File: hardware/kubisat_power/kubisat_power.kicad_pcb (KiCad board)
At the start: 2 copper layers, 80 x 80 mm, 83 parts, among them J1 USB_C_Receptacle_PowerOnly_6P, J2 B2B-PH-SM4-TB_LF__SN_, J3 B2B-PH-SM4-TB_LF__SN_, J4 B2B-PH-SM4-TB_LF__SN_, J5 B2B-PH-SM4-TB_LF__SN_, J6 Conn_01x04_Pin, J7 Conn_01x04_Pin, J8 Conn_01x04_Pin, Q1 Si2305, SW1 SW_Wuerth_450301014042, U2 INA3221, U3 LN2220, U4 CN3791, U5 TP4056, U6 DW01A, U7 FS8205

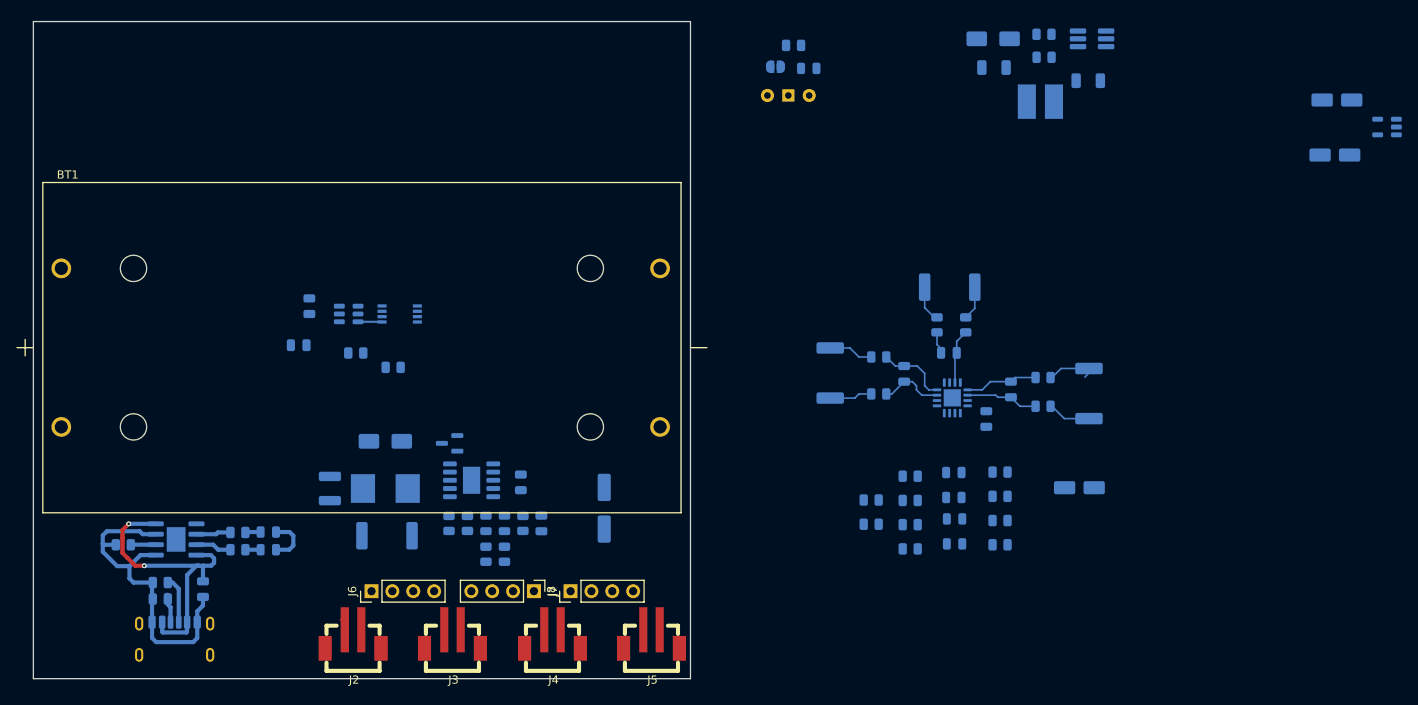
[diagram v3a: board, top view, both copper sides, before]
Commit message: arranged elements on board, made some traces
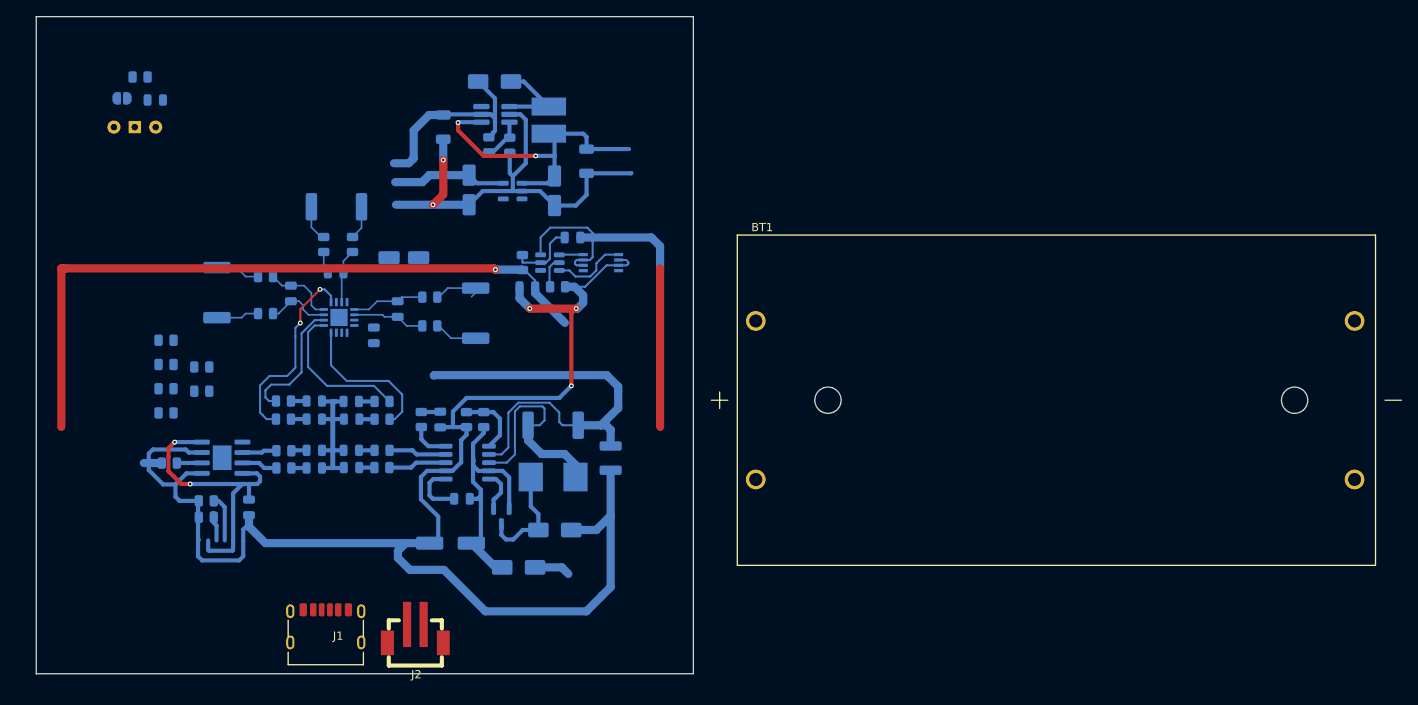
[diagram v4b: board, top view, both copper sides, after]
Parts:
- removed J3, J4, J5: B2B-PH-SM4-TB_LF__SN_, kubisat:B2B-PH-SM4-TB_LF__SN_
- removed J6, J7, J8: Conn_01x04_Pin, Connector_PinHeader_2.54mm:PinHeader_1x04_P2.54mm_Vertical
- added D12: SS14, Diode_SMD:D_SMA, B.Cu at (77.1, 84.2)
- J1: moved to F.Cu
- moved U1 106.7 mm to (76.4, 38.3)
- moved C8 105.5 mm to (71.1, 38.2), turned to -90 degrees
- moved C2 95.9 mm to (81.5, 38.3), turned to -90 degrees
- moved R27 92.1 mm to (34.2, 56.5)
- moved R28 92.1 mm to (34.2, 59.5)
- moved R29 92.1 mm to (34.2, 62.4)
- moved R30 92.1 mm to (34.2, 65.3)
- moved R36 89.0 mm to (48.5, 63.9)
- moved R33 87.5 mm to (48.5, 66.1)
- moved C7 86.9 mm to (63.1, 46.5)
- moved BT1 84.8 mm to (142.6, 63.8)
- moved R31 83.1 mm to (38.5, 59.8)
- moved R32 83.1 mm to (38.5, 62.7)
- moved D11 79.7 mm to (32.9, 27.2)
- moved JP1 79.7 mm to (28.8, 27.1)
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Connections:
- C2 pad 1: 5V_SENSE_OUT -> SOLAR_SENSE_OUT
- D10 pad 2: Net-(D10-A) -> INFO_LED_ENABLE
- D4 pad 2: Net-(D4-A) -> INFO_LED_ENABLE
- D5 pad 2: Net-(D5-A) -> INFO_LED_ENABLE
- D7 pad 2: Net-(D7-A) -> INFO_LED_ENABLE
- D8 pad 2: Net-(D8-A) -> INFO_LED_ENABLE
- D9 pad 2: Net-(D9-A) -> INFO_LED_ENABLE
- J2 pad 1: Net-(J6-Pin_3) -> GND
- J2 pad 2: VS -> Net-(D12-A)
- R23 pad 1: INFO_LED_ENABLE -> Net-(D4-K)
- R23 pad 2: Net-(D4-A) -> Net-(U4-~{DONE})
- R24 pad 1: INFO_LED_ENABLE -> Net-(D5-K)
- R24 pad 2: Net-(D5-A) -> Net-(U4-~{CHRG})
- R27 pad 1: Net-(D10-K) -> Net-(U2-PV)
- R28 pad 1: Net-(D9-K) -> Net-(U2-CRITICAL)
- R29 pad 1: Net-(D8-K) -> Net-(U2-WARNING)
- R30 pad 1: Net-(D7-K) -> Net-(U2-TC)
- R33 pad 1: INFO_LED_ENABLE -> Net-(D7-K)
- R33 pad 2: Net-(D7-A) -> Net-(U2-TC)
- R34 pad 1: INFO_LED_ENABLE -> Net-(D8-K)
- R34 pad 2: Net-(D8-A) -> Net-(U2-WARNING)
- R35 pad 1: INFO_LED_ENABLE -> Net-(D9-K)
- R35 pad 2: Net-(D9-A) -> Net-(U2-CRITICAL)
- R36 pad 1: INFO_LED_ENABLE -> Net-(D10-K)
- R36 pad 2: Net-(D10-A) -> Net-(U2-PV)
- U1 pad 1: 5V_SENSE_OUT -> SOLAR_SENSE_OUT
- U2 pad 10: Net-(D10-K) -> Net-(U2-PV)
- U2 pad 13: Net-(D7-K) -> Net-(U2-TC)
- U2 pad 8: Net-(D8-K) -> Net-(U2-WARNING)
- U2 pad 9: Net-(D9-K) -> Net-(U2-CRITICAL)
- U4 pad 3: Net-(D5-K) -> Net-(U4-~{CHRG})
- U4 pad 4: Net-(D4-K) -> Net-(U4-~{DONE})
- U7 pad 1: Net-(U6-GND) -> unconnected-(U7-D1-Pad1)
- U7 pad 2: unconnected-(U7-D12-Pad2) -> Net-(U6-GND)
- U7 pad 3: GND -> Net-(U6-GND)
- U7 pad 4: Net-(U6-OC) -> Net-(U6-OD)
- U7 pad 5: unconnected-(U7-D12-Pad5) -> Net-(U6-OC)
- U7 pad 6: Net-(U6-OD) -> GND
- U7 pad 7: (no net) -> GND
- U7 pad 8: (no net) -> unconnected-(U7-D2-Pad8)
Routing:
- net GND: track 40.9 -> 254.6 mm, vias 0 -> 5
- net SOLAR_SENSE_OUT: track 9.69 -> 132.4 mm, vias 0 -> 3
- net SOLAR_SENSE_IN: track 5.46 -> 58.0 mm
- net Net-(U6-GND): track 2.94 -> 49.9 mm
- net VS: track 1.47 -> 33.0 mm
- net Net-(U4-CSP): track 0.00 -> 26.8 mm
- net 5V_SENSE_IN: track 5.30 -> 30.8 mm
- net Net-(U2-TC): track 0.00 -> 24.0 mm, vias 0 -> 2
- net INFO_LED_ENABLE: track 5.82 -> 27.0 mm
- net Net-(U2-CRITICAL): track 0.00 -> 18.1 mm
- net Net-(U2-WARNING): track 0.00 -> 18.1 mm
- net Net-(U2-PV): track 0.00 -> 15.7 mm
- net +3V3: track 0.00 -> 13.9 mm
- net Net-(D6-K): track 0.00 -> 13.3 mm
- net Net-(D1-A): track 0.00 -> 10.7 mm
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
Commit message: more traces
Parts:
- removed SW1: SW_Wuerth_450301014042, Button_Switch_THT:SW_Slide-03_Wuerth-WS-SLTV_10x2.5x6.4_P2.54mm
- added J3: Conn_01x08_MountingPin, Connector_JST:JST_PH_S8B-PH-SM4-TB_1x08-1MP_P2.00mm_Horizontal, F.Cu at (49.8, 24.2)
- moved R37 58.2 mm to (55.6, 77.2)
- moved D11 56.6 mm to (59.5, 77.2)
- moved JP1 55.2 mm to (51.9, 77.2), turned to 0 degrees
- moved R32 20.7 mm to (58.7, 58.1)
- moved R31 20.1 mm to (58.6, 60.2)
- moved R29 12.8 mm to (46.5, 58.9)
- moved R27 12.4 mm to (46.5, 56.6)
- moved R28 8.67 mm to (42.6, 61.4)
- moved R30 8.57 mm to (42.6, 64.0)
- moved C7 1.35 mm to (61.9, 46.8), turned to 0 degrees
- moved C6 0.72 mm to (59.6, 55.2), turned to 90 degrees
- moved C11 0.11 mm to (44.2, 76.9)
- moved R14 0.11 mm to (34.5, 71.5)
- moved R17 0.11 mm to (39.0, 78.1)
- moved R18 0.11 mm to (39.0, 76.1)
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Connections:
- R10 pad 1: 5V_SENSE_OUT -> SOLAR_SENSE_OUT
- R11 pad 1: 5V_SENSE_IN -> SOLAR_SENSE_IN
- R11 pad 2: 5V_SENSE_OUT -> SOLAR_SENSE_OUT
- R3 pad 1: SOLAR_SENSE_IN -> USB_SENSE_IN
- R5 pad 1: SOLAR_SENSE_IN -> USB_SENSE_IN
- R6 pad 1: USB_SENSE_IN -> 5V_SENSE_IN
- R7 pad 1: SOLAR_SENSE_OUT -> 5V_SENSE_OUT
- R8 pad 1: SOLAR_SENSE_OUT -> 5V_SENSE_OUT
- R8 pad 2: USB_SENSE_IN -> 5V_SENSE_IN
- R9 pad 1: 5V_SENSE_IN -> SOLAR_SENSE_IN
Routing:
- net 5V_SENSE_OUT: track 6.39 -> 176.5 mm, vias 0 -> 8
- net GND: track 254.6 -> 330.3 mm, vias 5 -> 13
- net SOLAR_SENSE_OUT: track 132.4 -> 198.3 mm, vias 3 -> 4
- net INA3221_SDA: track 0.00 -> 59.2 mm, vias 0 -> 3
- net INA3221_SCL: track 0.00 -> 48.0 mm, vias 0 -> 3
- net USB_SENSE_IN: track 4.13 -> 47.0 mm, vias 0 -> 2
- net +3V3: track 13.9 -> 31.3 mm, vias 0 -> 1
- net Net-(U2-CRITICAL): track 18.1 -> 27.2 mm, vias 0 -> 2
- net 5V_SENSE_IN: track 30.8 -> 38.5 mm
- net INFO_LED_ENABLE: track 27.0 -> 34.4 mm
- net Net-(U2-WARNING): track 18.1 -> 25.2 mm, vias 0 -> 2
- net Net-(U2-IN-2): track 2.71 -> 6.75 mm
- net Net-(U2-PV): track 15.7 -> 19.2 mm, vias 0 -> 2
- net Net-(U2-TC): track 24.0 -> 26.6 mm
- net Net-(D11-A): track 0.00 -> 1.95 mm

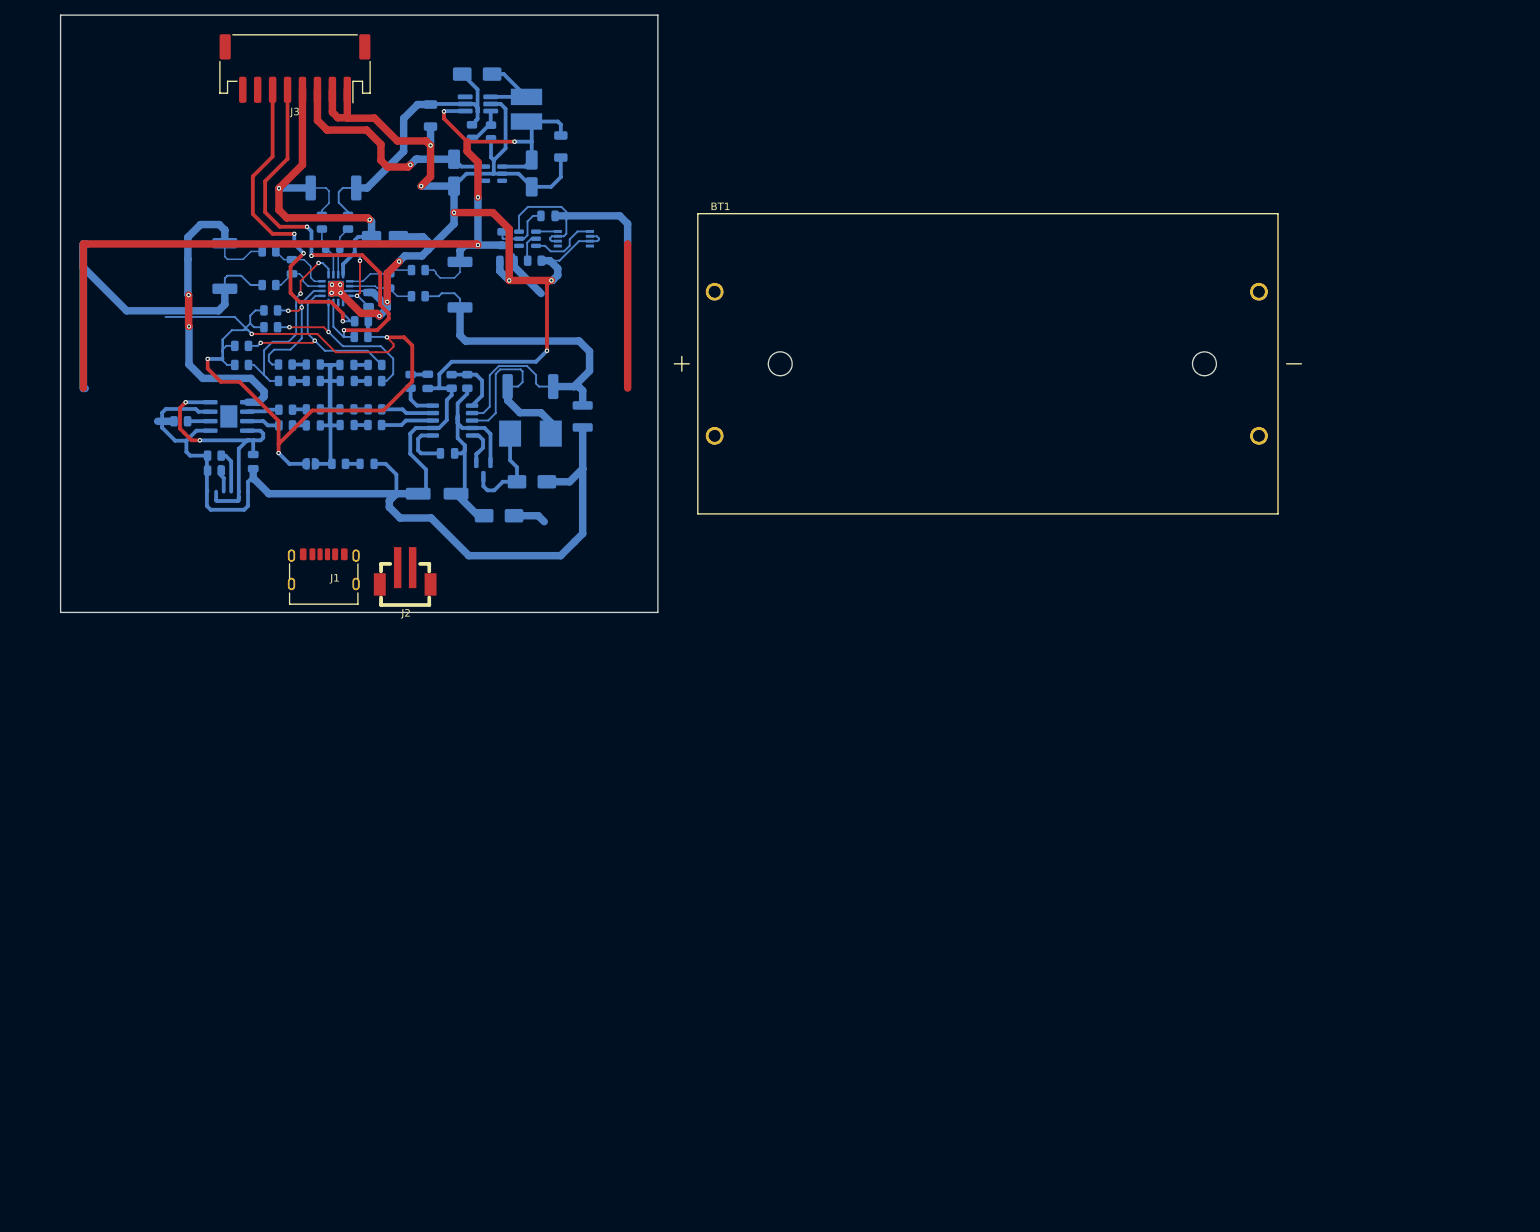
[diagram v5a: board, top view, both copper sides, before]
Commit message: complete routing, changed usb and side terminal - this version was ordered in jlcpcb
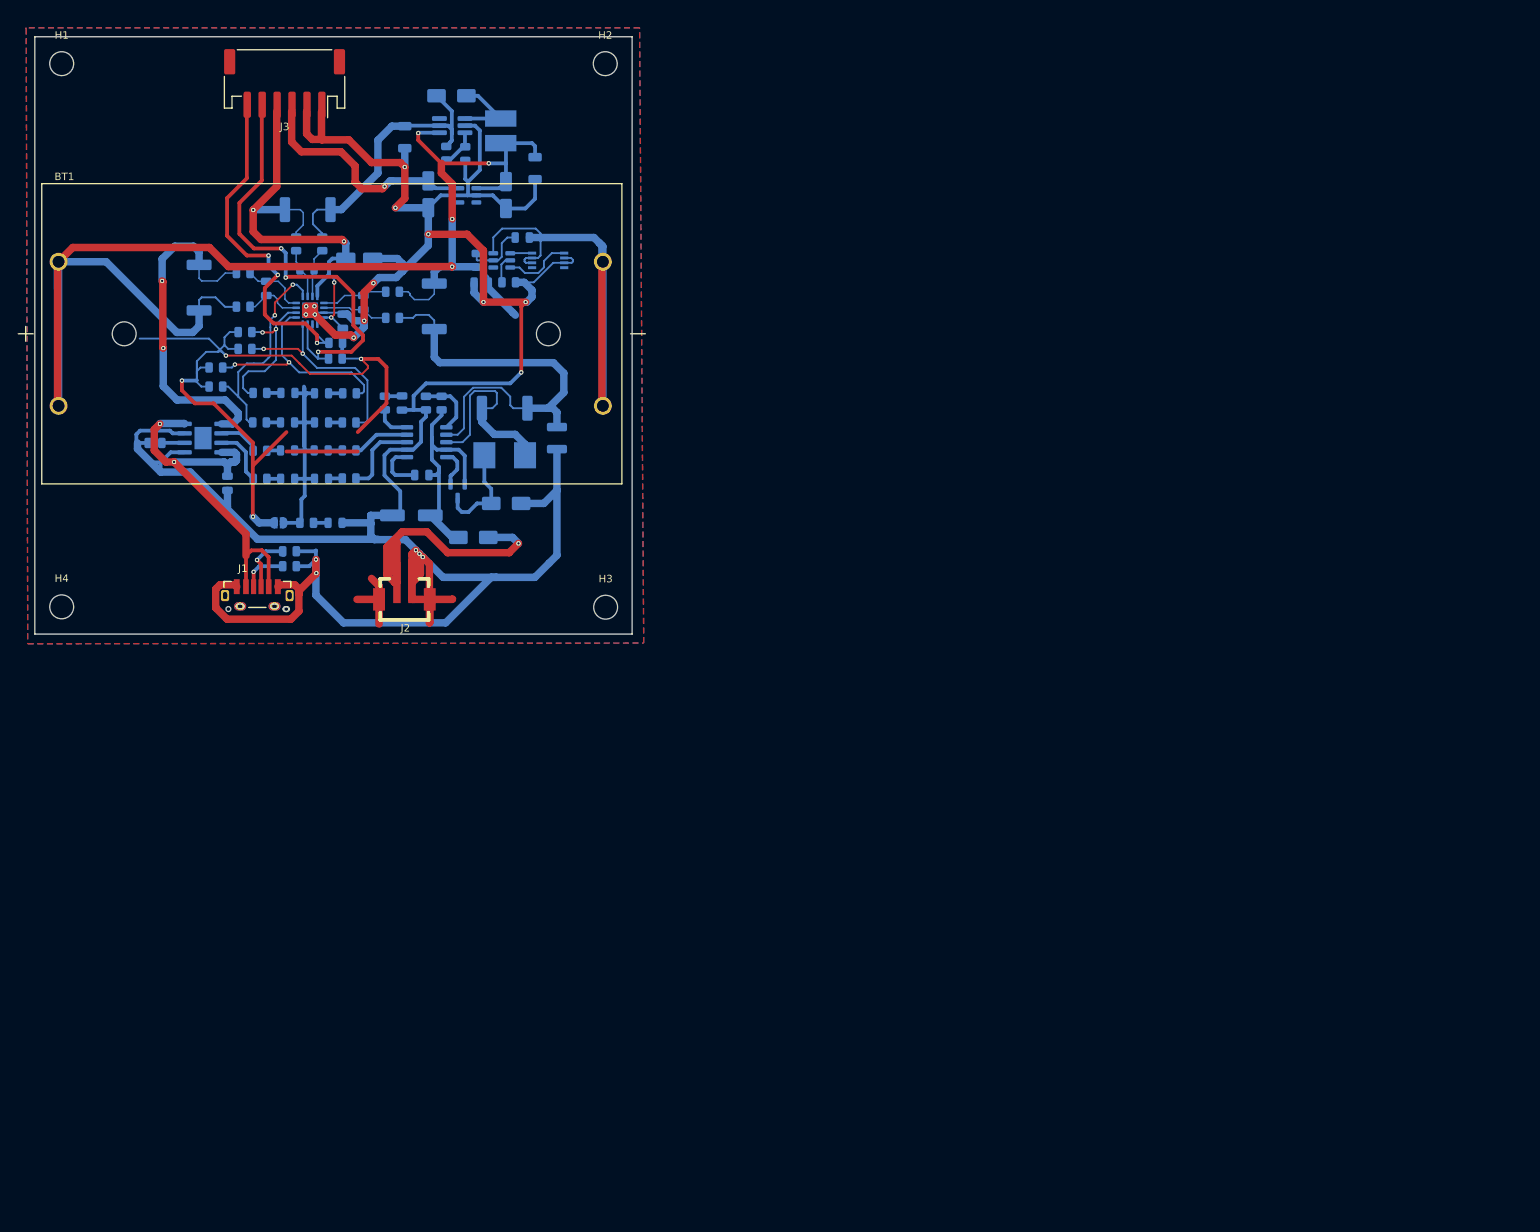
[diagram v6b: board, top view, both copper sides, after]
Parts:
- added H1: MountingHole, MountingHole:MountingHole_3.2mm_M3_DIN965, F.Cu at (18.6, 23.6)
- added H2: MountingHole, MountingHole:MountingHole_3.2mm_M3_DIN965, F.Cu at (91.3, 23.6)
- added H3: MountingHole, MountingHole:MountingHole_3.2mm_M3_DIN965, F.Cu at (91.4, 96.4)
- added H4: MountingHole, MountingHole:MountingHole_3.2mm_M3_DIN965, F.Cu at (18.6, 96.3)
- J1: footprint Connector_USB:USB_C_Receptacle_HRO_TYPE-C-31-M-17 -> Connector_USB:GCT_USB4140-GF-0230-C_REV0.4
- J3: value Conn_01x08_MountingPin -> Conn_01x06_MountingPin; footprint Connector_JST:JST_PH_S8B-PH-SM4-TB_1x08-1MP_P2.00mm_Horizontal -> Connector_JST:JST_PH_S6B-PH-SM4-TB_1x06-1MP_P2.00mm_Horizontal
- moved BT1 88.0 mm to (54.7, 59.8)
- moved R18 17.9 mm to (49.1, 90.9), turned to 0 degrees
- moved R17 14.8 mm to (49.1, 88.9), turned to 0 degrees
- moved J1 9.21 mm to (44.8, 94.8)
- moved D11 8.99 mm to (55.2, 85.1)
- moved JP1 8.99 mm to (47.6, 85.1)
- moved R37 8.99 mm to (51.4, 85.1)
- moved D5 7.98 mm to (53.4, 79.2)
- moved D2 7.93 mm to (48.8, 79.2)
- moved R16 7.93 mm to (45.1, 79.2)
- moved R24 7.93 mm to (57.0, 79.2)
- moved D7 6.53 mm to (48.8, 71.7)
- moved R33 6.53 mm to (45.0, 71.7)
- moved D8 6.53 mm to (53.4, 71.7)
- moved R34 6.53 mm to (57.0, 71.7)
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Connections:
- J1 pad S1: unconnected-(J1-SHIELD-PadS1) -> GND
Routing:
- net GND: track 330.3 -> 439.0 mm, vias 13 -> 18
- net Net-(D12-A): track 4.38 -> 39.4 mm, vias 0 -> 1
- net Net-(U5-CE): track 37.0 -> 64.3 mm
- net SOLAR_SENSE_OUT: track 198.3 -> 220.9 mm
- net Net-(U6-GND): track 49.9 -> 72.0 mm
- net INFO_LED_ENABLE: track 34.4 -> 39.8 mm
- net 5V_SENSE_OUT: track 176.5 -> 181.0 mm
- net Net-(J1-CC2): track 3.62 -> 7.88 mm, vias 0 -> 1
- net Net-(U4-~{CHRG}): track 7.10 -> 10.8 mm
- net Net-(U5-~{CHRG}): track 4.39 -> 7.76 mm
- net Net-(U2-WARNING): track 25.2 -> 28.3 mm
- net Net-(U2-CRITICAL): track 27.2 -> 30.2 mm
- net Net-(U2-TC): track 26.6 -> 28.9 mm
- net Net-(U5-~{STDBY}): track 4.22 -> 5.49 mm
- net Net-(U2-PV): track 19.2 -> 20.0 mm
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- added copper zone on B.Cu, net GND
- added copper zone on F.Cu, net GND
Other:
- board text added: "CHARGE"
- board text added: "CRIT"
- board text added: "DONE"
- board text added: "PV"
- board text added: "SOLAR"
- board text added: "TC"
- board text added: "USB"
- board text added: "WARN"
